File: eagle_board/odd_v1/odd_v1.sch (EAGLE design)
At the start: 19 parts

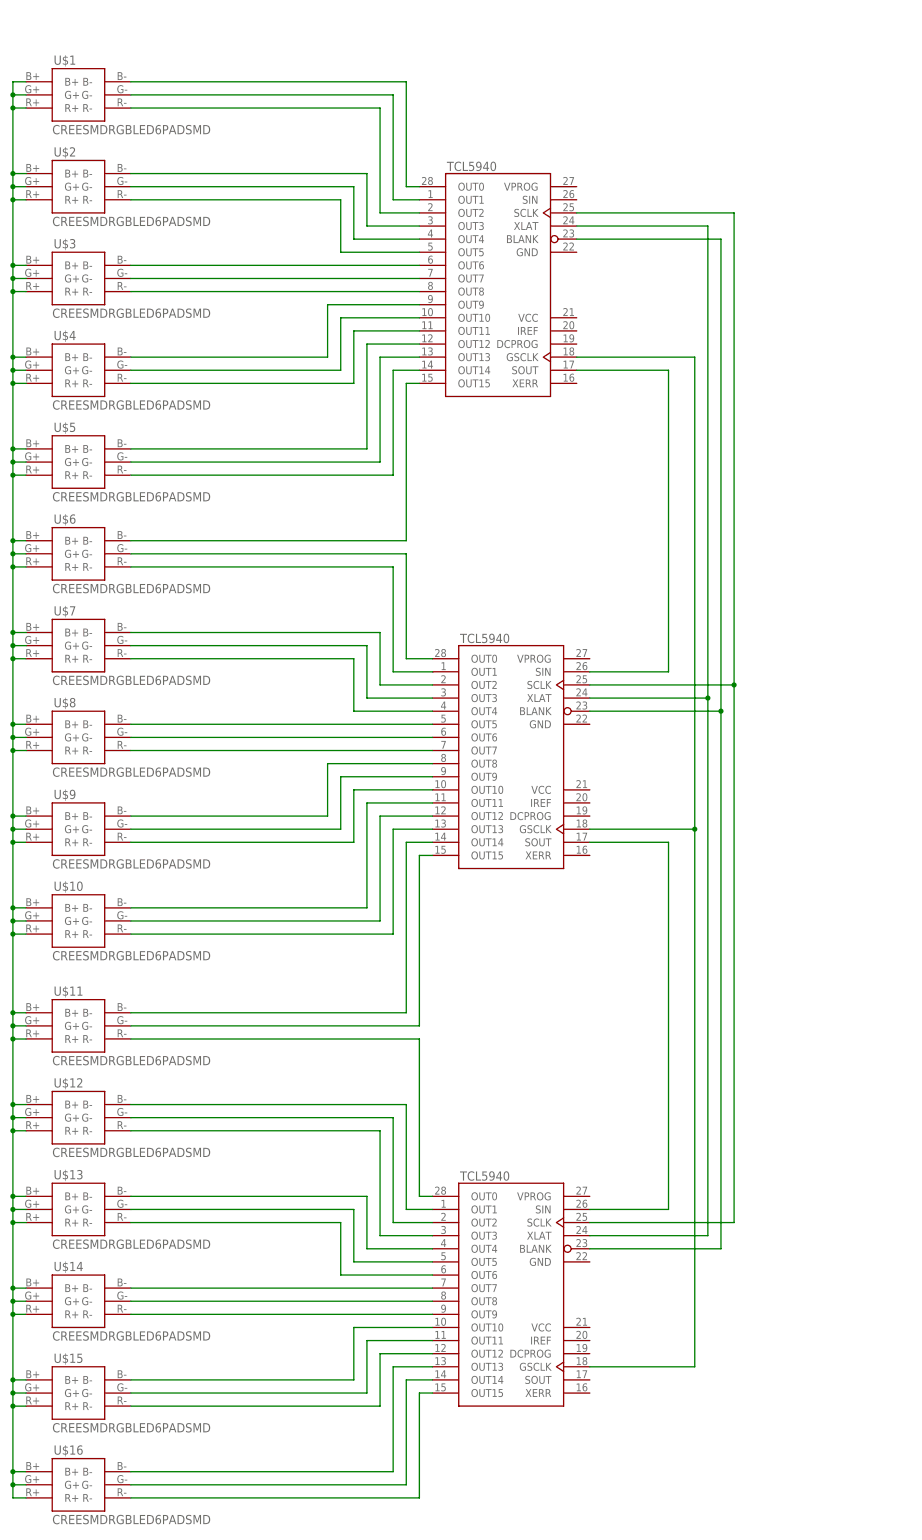
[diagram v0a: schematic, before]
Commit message: Updated board, all desired connections in schematic have been made.
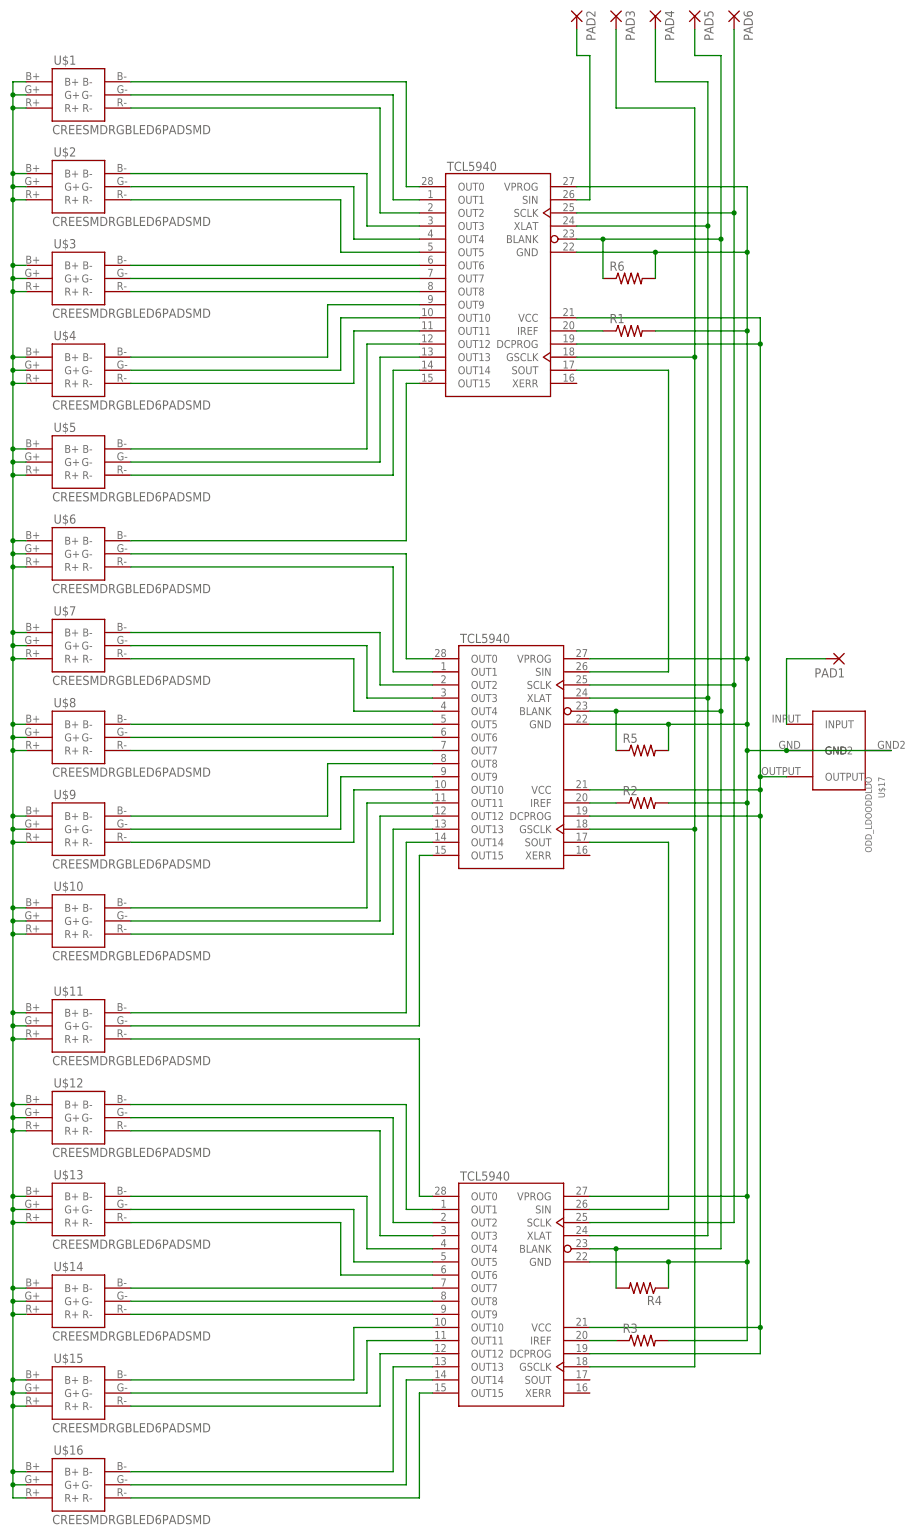
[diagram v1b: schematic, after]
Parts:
- added PAD1, PAD2, PAD3, PAD4, PAD5, PAD6: (no value), wirepad:2,54/1,1
- added R1, R2, R3, R4, R5, R6: (no value), resistor:R-US_0204/7
- added U$17: ODD_LDOODDLDO, ODD_LDO:ODD_LDOODDLDO
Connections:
- new net N$56: IC1.GND, IC1.VPROG, IC2.GND, IC2.VPROG, IC3.GND, IC3.VPROG, R1.2, R2.2, R3.2, R4.1, R5.2, R6.2, U$17.GND, U$17.GND2
- new net N$57: IC1.DCPROG, IC1.VCC, IC2.DCPROG, IC2.VCC, IC3.DCPROG, IC3.VCC, U$17.OUTPUT
- new net N$58: IC1.IREF, R1.1
- new net N$59: IC2.IREF, R2.1
- new net N$60: IC3.IREF, R3.1
- new net N$61: PAD1.P, U$17.INPUT
- new net N$62: IC1.SIN, PAD2.P
- net N$52: now also PAD3.P
- net N$53: now also PAD4.P
- net N$54: now also PAD5.P, R4.2, R5.1, R6.1
- net N$55: now also PAD6.P
